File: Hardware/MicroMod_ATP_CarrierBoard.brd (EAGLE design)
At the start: 86.4 x 55.9 mm, 216 parts, among them J19 QWIIC_RIGHT_ANGLE, J2 JTAG, J20 QWIIC_RIGHT_ANGLE, J21 1X04_SMD_STRAIGHT_COMBO, J4 USB_A_SMT_FEMALE, J6 MICROMOD-2222-C, J8 1X04_SMD_STRAIGHT_COMBO, U5 AP7361C-33

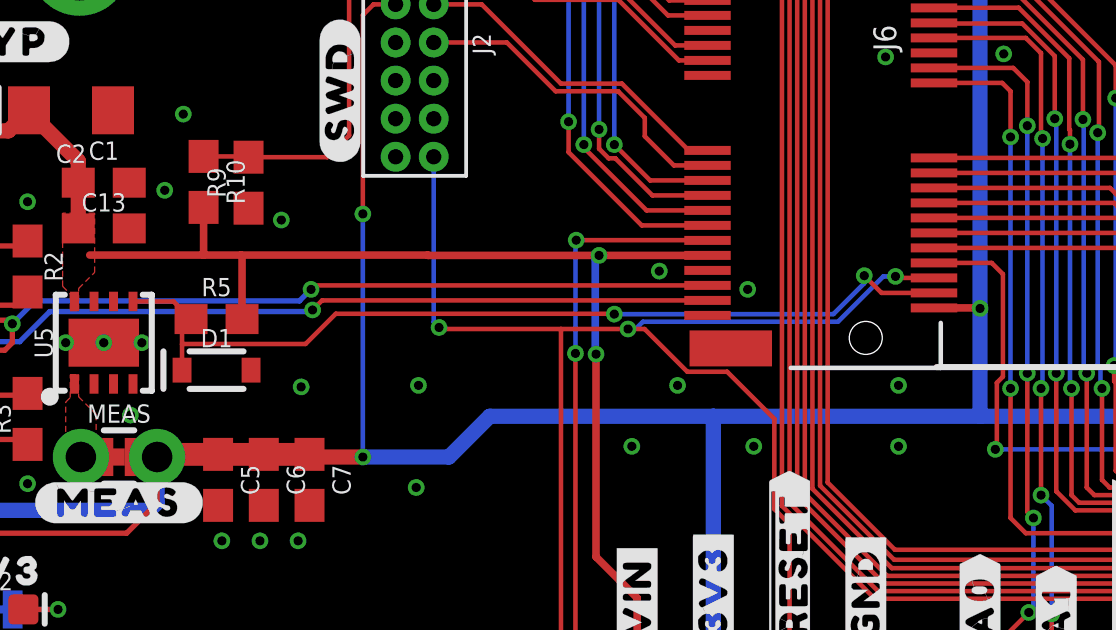
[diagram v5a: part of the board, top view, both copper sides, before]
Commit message: Adds a normally open enable jumper to 3.3V EN
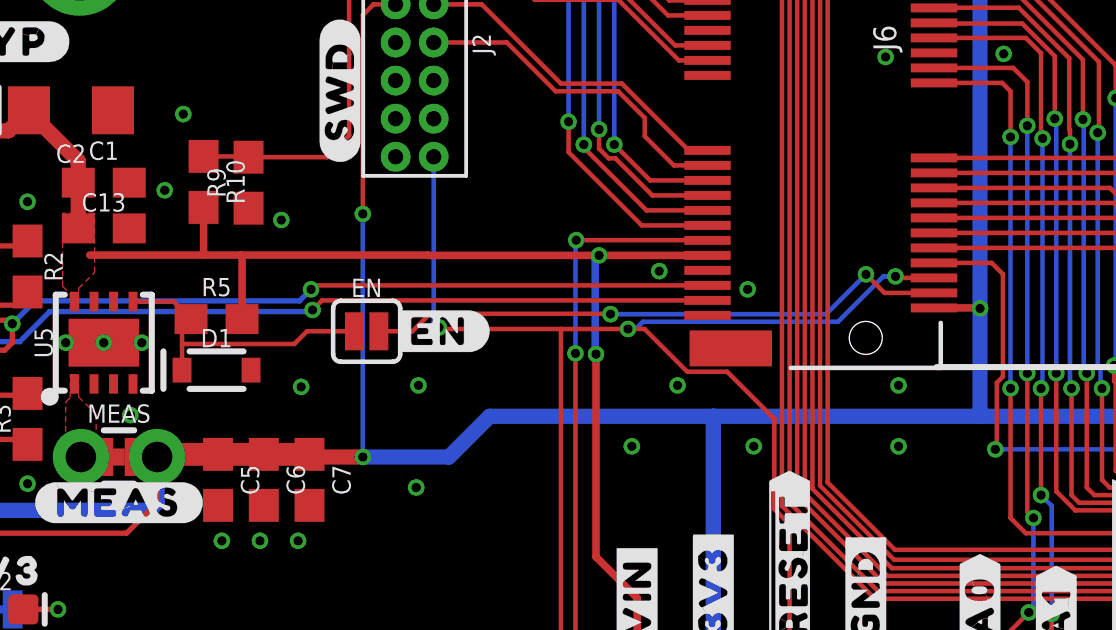
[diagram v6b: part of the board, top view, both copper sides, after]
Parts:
- added EN: JUMPER-SMT_2_NO_SILK, SparkFun-Jumpers:SMT-JUMPER_2_NO_SILK
- added U$48: (no value), output:#EN#0
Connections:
- new net N$5: EN.2, J6.4
- net 3.3V_EN: now also EN.1; no longer J6.4
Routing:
- net 3.3V_EN: track 30.5 -> 10.0 mm, vias 2 -> 0
- net N$5: track 0.00 -> 19.6 mm, vias 0 -> 2
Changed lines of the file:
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@@
 <element name="LOGO2" library="SparkFun-Aesthetics" package="QWIIC_5MM" value="QWIIC_LOGO_5MM" x="68.326" y="23.368" smashed="yes" rot="MR0"/>
 <element name="TP1" library="SparkFun-Connectors" package="PAD.03X.05" value="TEST-POINT3X5" x="58.42" y="35.56" smashed="yes" rot="MR0"/>
+<element name="EN" library="SparkFun-Jumpers" package="SMT-JUMPER_2_NO_SILK" package3d_urn="urn:adsk.eagle:package:39279/1" value="JUMPER-SMT_2_NO_SILK" x="18.923" y="18.161" smashed="yes">
+<attribute name="NAME" x="18.923" y="19.304" size="0.6096" layer="25" font="vector" ratio="20" align="bottom-center"/>
+<attribute name="VALUE" x="18.923" y="17.018" size="0.6096" layer="27" font="vector" ratio="20" align="top-center"/>
+</element>
+<element name="U$48" library="output" package="#EN#0" value="" x="21.336" y="18.161" smashed="yes"/>
 </elements>
 <signals>
@@
 <contactref element="D1" pad="C"/>
 <contactref element="R5" pad="1"/>
-<contactref element="J6" pad="4"/>
 <wire x1="11.135" y1="19.155" x2="12.4816" y2="19.155" width="0.1524" layer="1"/>
 <wire x1="12.4816" y1="19.155" x2="12.8973" y2="18.7393" width="0.1524" layer="1"/>
 <wire x1="12.8973" y1="18.7393" x2="13.0692" y2="18.5674" width="0.1524" layer="1"/>
-<wire x1="27.178" y1="18.7328" x2="27.0764" y2="18.7328" width="0.1524" layer="1"/>
-<wire x1="27.0764" y1="18.7328" x2="27.064" y2="18.7452" width="0.1524" layer="1"/>
-<via x="27.178" y="18.7328" extent="1-16" drill="0.3048"/>
-<wire x1="27.178" y1="18.7328" x2="34.4808" y2="18.7328" width="0.1524" layer="16"/>
-<wire x1="35.5092" y1="19.7612" x2="35.5092" y2="20.0152" width="0.1524" layer="16"/>
-<via x="35.5092" y="20.0152" extent="1-16" drill="0.3048"/>
-<wire x1="35.5092" y1="20.0152" x2="36.0844" y2="19.44" width="0.1524" layer="1"/>
-<wire x1="36.0844" y1="19.44" x2="37.835" y2="19.44" width="0.1524" layer="1"/>
-<wire x1="34.4808" y1="18.7328" x2="35.5092" y2="19.7612" width="0.1524" layer="16"/>
-<wire x1="17.89318125" y1="18.7452" x2="16.88518125" y2="17.7372" width="0.1524" layer="1"/>
-<wire x1="27.064" y1="18.7452" x2="17.89318125" y2="18.7452" width="0.1524" layer="1"/>
 <wire x1="12.7692" y1="16.8656" x2="12.7692" y2="17.7292" width="0.1524" layer="1"/>
 <wire x1="12.7692" y1="17.7292" x2="12.7692" y2="18.6112" width="0.1524" layer="1"/>
 <wire x1="12.7692" y1="18.6112" x2="12.8973" y2="18.7393" width="0.1524" layer="1"/>
 <wire x1="12.7772" y1="17.7372" x2="12.7692" y2="17.7292" width="0.1524" layer="1"/>
-<wire x1="16.88518125" y1="17.7372" x2="12.7772" y2="17.7372" width="0.1524" layer="1"/>
+<wire x1="12.7772" y1="17.7372" x2="16.51" y2="17.7372" width="0.1524" layer="1"/>
+<contactref element="EN" pad="1"/>
+<wire x1="16.51" y1="17.7372" x2="16.9338" y2="18.161" width="0.1524" layer="1"/>
+<wire x1="16.9338" y1="18.161" x2="18.5166" y2="18.161" width="0.1524" layer="1"/>
 </signal>
 <signal name="G1">
@@
 <signal name="N$6">
 </signal>
+<signal name="N$5">
+<contactref element="J6" pad="4"/>
+<contactref element="EN" pad="2"/>
+<wire x1="37.835" y1="19.44" x2="36.186" y2="19.44" width="0.1524" layer="1"/>
+<wire x1="36.186" y1="19.44" x2="35.566909375" y2="20.059090625" width="0.1524" layer="1"/>
+<via x="35.566909375" y="20.059090625" extent="1-16" drill="0.3048"/>
+<wire x1="35.566909375" y1="20.059090625" x2="34.24061875" y2="18.7328" width="0.1524" layer="16"/>
+<via x="27.051" y="18.7328" extent="1-16" drill="0.3048"/>
+<wire x1="27.051" y1="18.7328" x2="27.0386" y2="18.7452" width="0.1524" layer="1"/>
+<wire x1="27.0386" y1="18.7452" x2="21.0312" y2="18.7452" width="0.1524" layer="1"/>
+<wire x1="34.24061875" y1="18.7328" x2="27.051" y2="18.7328" width="0.1524" layer="16"/>
+<wire x1="19.3294" y1="18.161" x2="20.447" y2="18.161" width="0.1524" layer="1"/>
+<wire x1="20.447" y1="18.161" x2="21.0312" y2="18.7452" width="0.1524" layer="1"/>
+</signal>
 </signals>

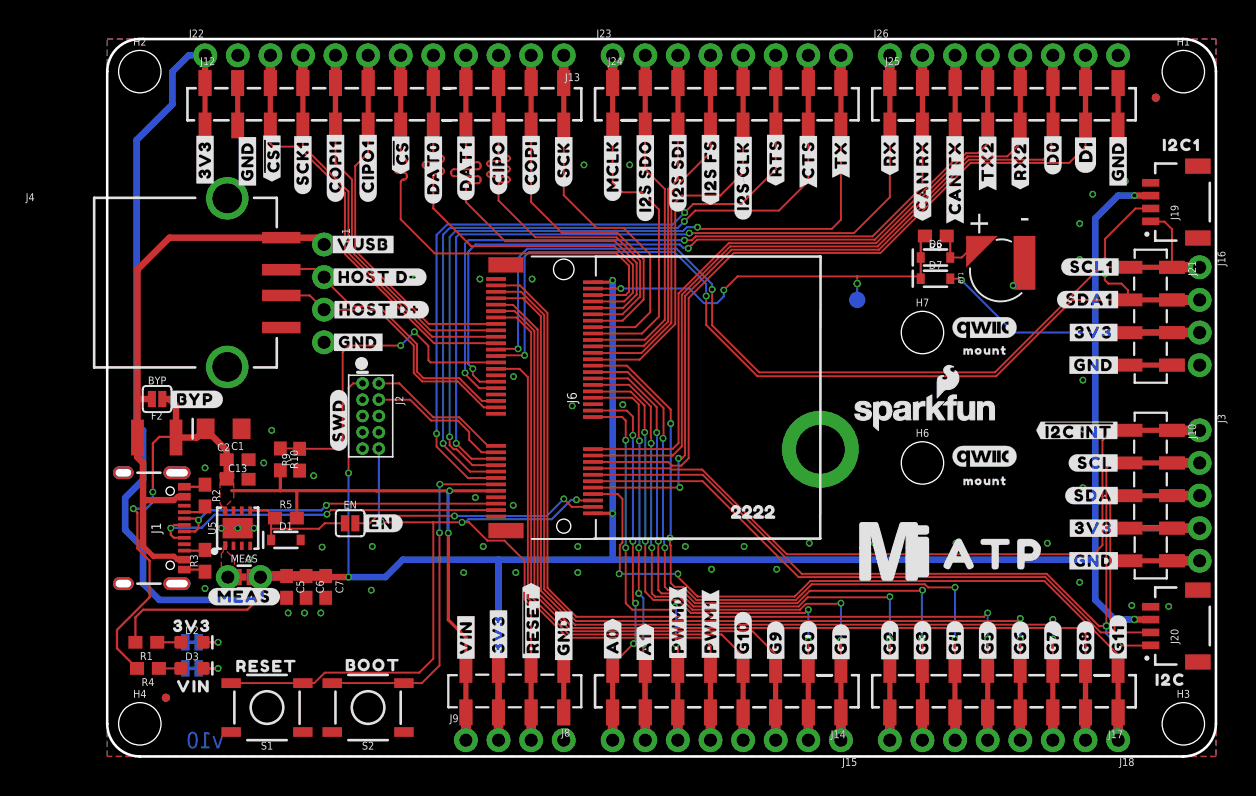
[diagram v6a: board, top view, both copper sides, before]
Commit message: Gives some space in between data lines
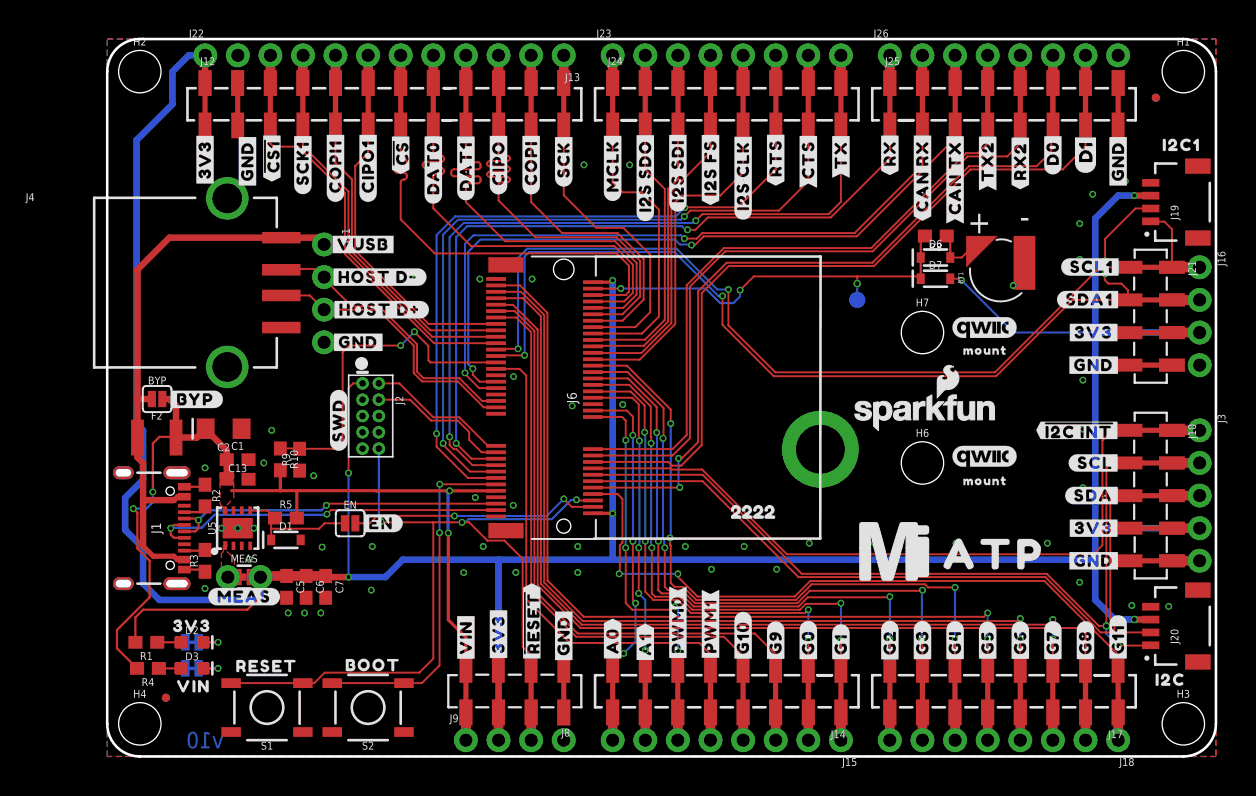
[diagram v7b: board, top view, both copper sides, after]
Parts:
- moved U$37 0.06 mm to (33.1, 10.4)
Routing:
- net RX1: track 68.0 -> 66.4 mm
- net TX1: track 64.4 -> 63.5 mm
- net CAN_TXO: track 63.2 -> 62.3 mm
- net CAN_RXI: track 62.9 -> 62.1 mm
- net SDA1: track 83.9 -> 83.4 mm

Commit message: Adds a diode with 220mV Vf to protect back voltage from USB-Host (just in case)
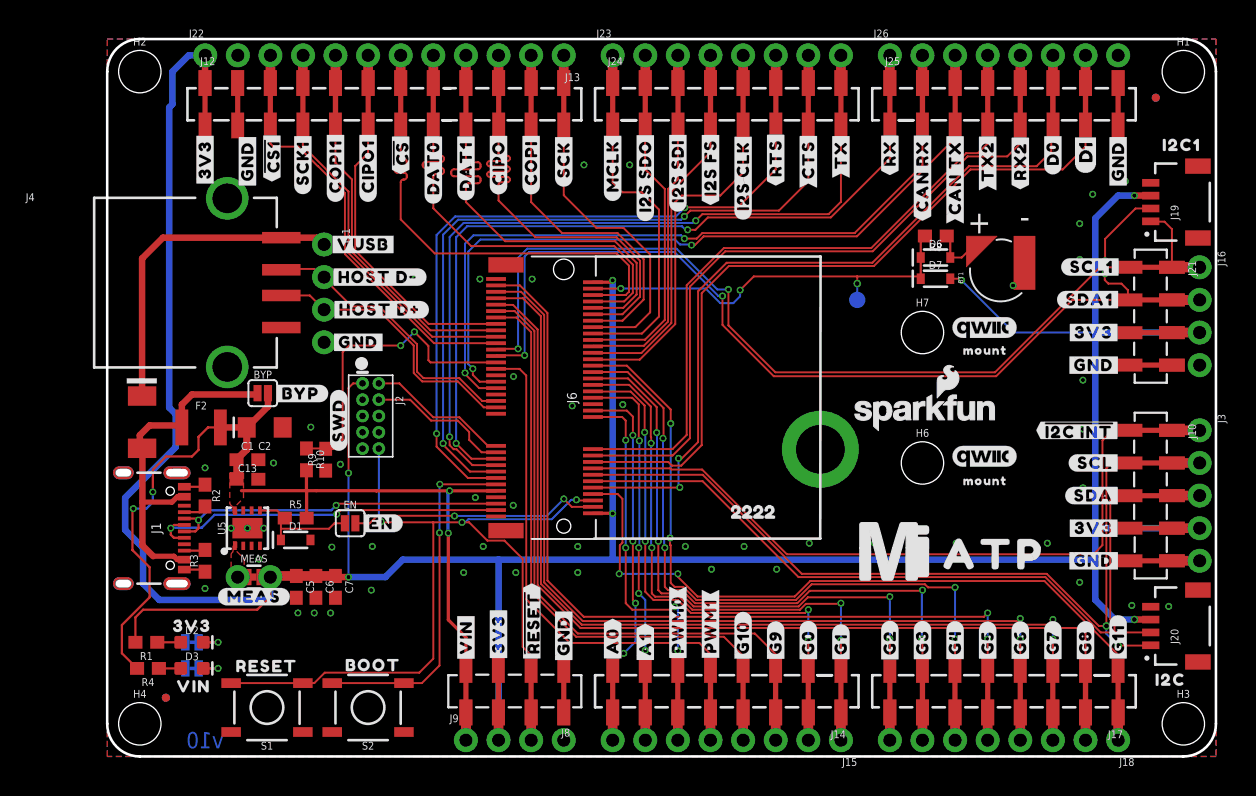
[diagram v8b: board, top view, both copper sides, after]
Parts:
- added D4: 1A/15V/220mV, SparkFun-DiscreteSemi:DO-214BA
- moved BYP 8.24 mm to (12.1, 28.3)
- moved U$39 8.22 mm to (15.1, 28.3)
- moved F2 3.54 mm to (7.32, 25.6)
- moved C2 3.20 mm to (12.3, 25.6)
- moved R10 2.03 mm to (15.5, 23.1)
- moved R9 2.03 mm to (17.0, 23.1)
- moved C1 0.76 mm to (10.9, 23.1)
- moved C13 0.76 mm to (10.9, 21.6)
- moved C6 0.76 mm to (16.3, 13.2)
- moved C7 0.76 mm to (17.8, 13.2)
- moved D1 0.76 mm to (14.7, 16.9)
- moved MEAS 0.76 mm to (11.4, 14.0)
- moved R5 0.76 mm to (14.7, 18.6)
- moved U$132 0.76 mm to (11.4, 12.4)
- moved U$42 0.76 mm to (11.4, 12.4)
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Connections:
- new net N$7: D4.C, J11.1, J4.VBUS
- net V_USB: now also D4.A; no longer J11.1, J4.VBUS
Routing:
- net N$7: track 0.00 -> 25.8 mm
- net V_USB: track 45.7 -> 27.5 mm
- net VIN/3: track 26.2 -> 24.2 mm
- net VIN: track 80.9 -> 81.8 mm
- net 3.3V: track 269.7 -> 270.4 mm
- net 3.3V_EN: track 10.0 -> 9.27 mm
